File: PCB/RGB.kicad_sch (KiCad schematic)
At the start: 30 parts

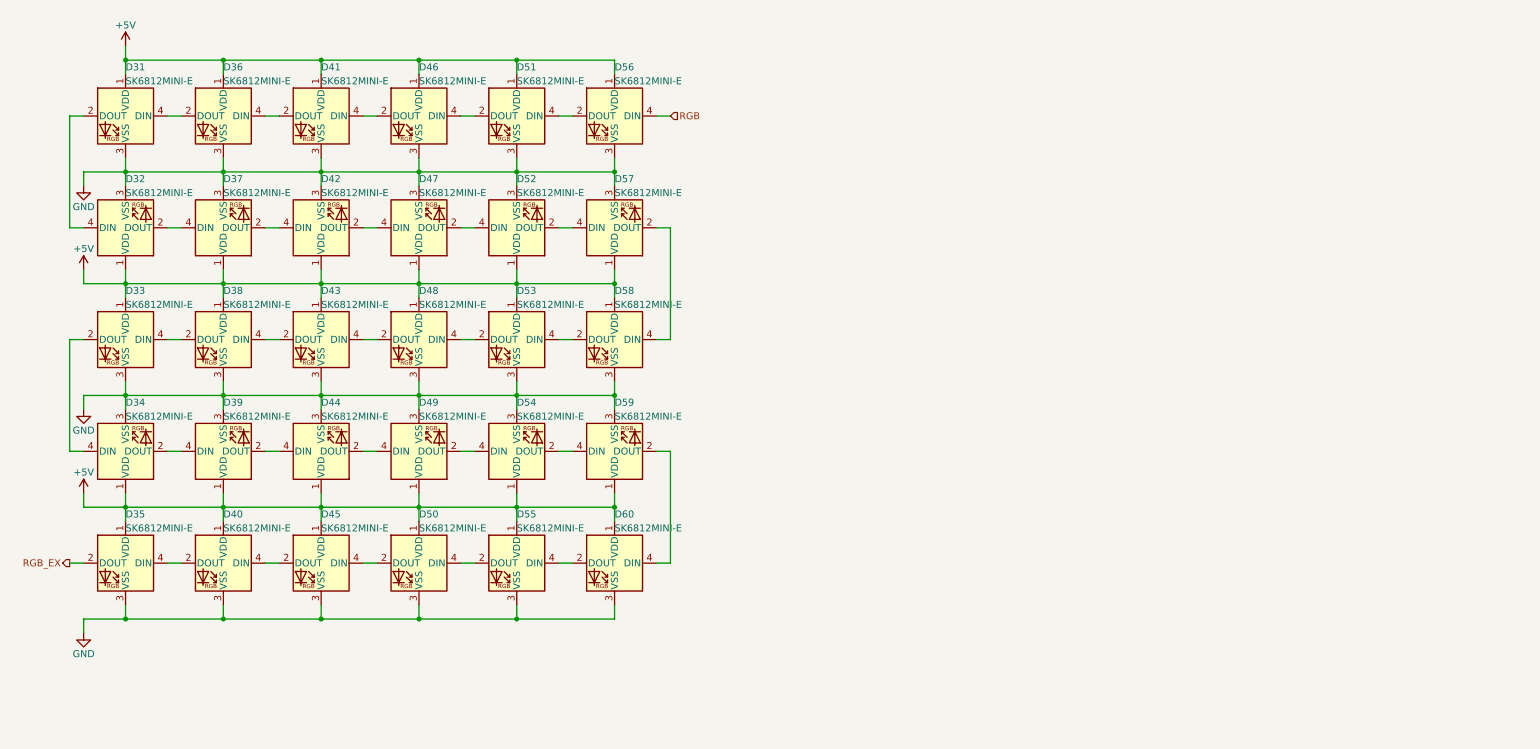
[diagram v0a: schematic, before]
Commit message: 08/08/2023 update
Removed Ogen footprint, and future VIK support is planned. Rerouted board following latest Honeydew revision. WIP support for the USB2541 is added, but it's very tentative and not yet complete. Added CX70M-24P1 footprint.
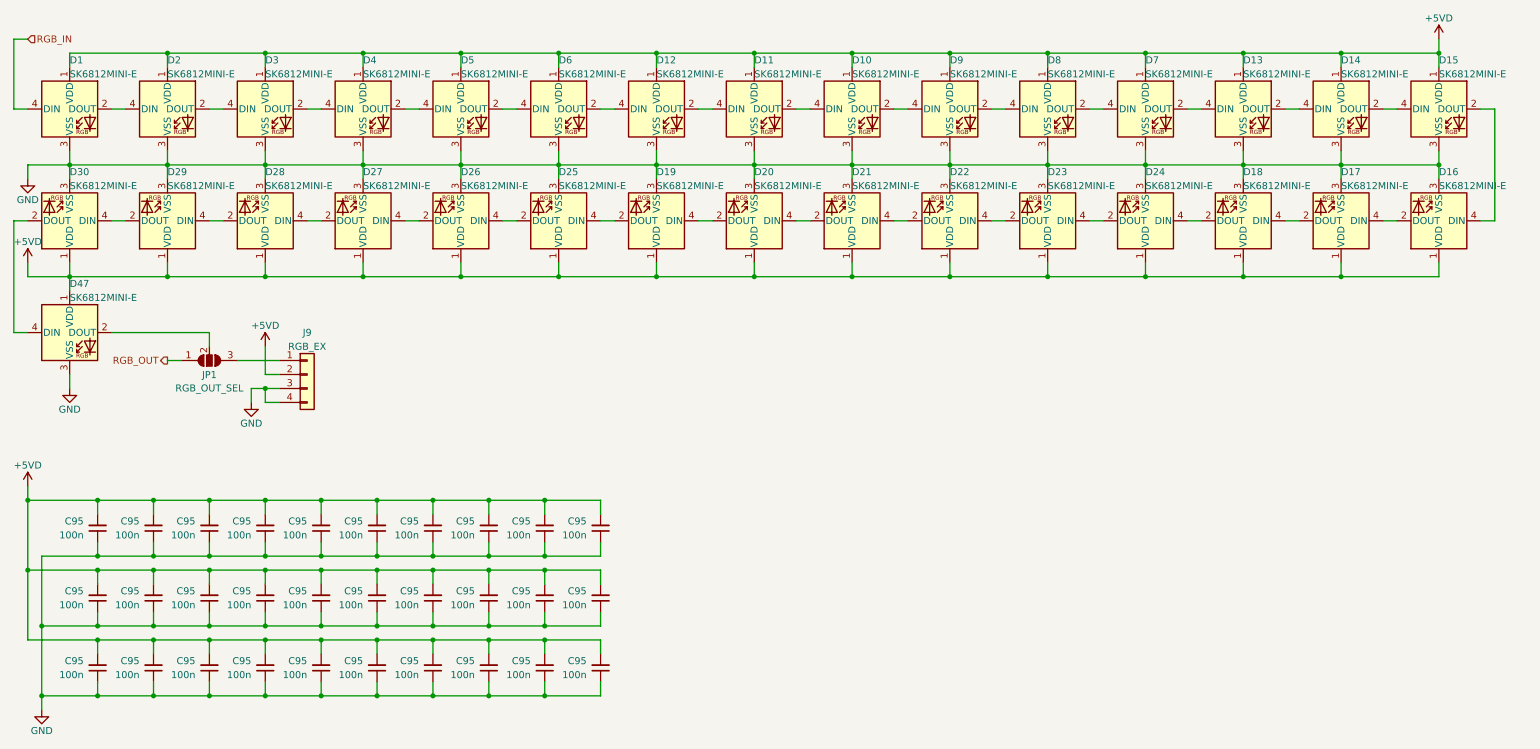
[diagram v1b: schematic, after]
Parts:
- removed D31, D32, D33, D34, D35, D36, D37, D38, D39, D40, D41, D42, D43, D44, D45, D46, D48, D49, D50, D51, D52, D53, D54, D55, D56, D57, D58, D59, D60: SK6812MINI-E, Cantaloupe:YS-SK6812MINI-E-Flippable, symbol Honeydew:SK6812MINI-E
- added C95 (x30): 100n, Cantaloupe:C_0402_1005Metric, symbol Device:C_Small
- added D1, D10, D11, D12, D13, D14, D15, D16, D17, D18, D19, D2, D20, D21, D22, D23, D24, D25, D26, D27, D28, D29, D3, D30, D4, D5, D6, D7, D8, D9: SK6812MINI-E, Cantaloupe:YS-SK6812MINI-E, symbol Honeydew:SK6812MINI-E
- added J9: RGB_EX, Cantaloupe:Header_RGB, symbol Connector_Generic:Conn_01x04
- added JP1: RGB_OUT_SEL, Jumper:SolderJumper-3_P1.3mm_Open_Pad1.0x1.5mm_NumberLabels, symbol Honeydew:SolderJumper_3_Open
- D47: footprint Cantaloupe:YS-SK6812MINI-E-Flippable -> Cantaloupe:YS-SK6812MINI-E; LCSC C5149201 -> C524051
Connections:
- net GND: now also C95.1, C95.1, C95.1, C95.1, C95.1, C95.1, C95.1, C95.1, C95.1, C95.1, C95.1, C95.1, C95.1, C95.1, C95.1, C95.1, C95.1, C95.1, C95.1, C95.1, C95.1, C95.1, C95.1, C95.1, C95.1, C95.1, C95.1, C95.1, C95.1, C95.1, D1.3 (VSS), D10.3 (VSS), D11.3 (VSS), D12.3 (VSS), D13.3 (VSS), D14.3 (VSS), D15.3 (VSS), D16.3 (VSS), D17.3 (VSS), D18.3 (VSS), D19.3 (VSS), D2.3 (VSS), D20.3 (VSS), D21.3 (VSS), D22.3 (VSS), D23.3 (VSS), D24.3 (VSS), D25.3 (VSS), D26.3 (VSS), D27.3 (VSS), D28.3 (VSS), D29.3 (VSS), D3.3 (VSS), D30.3 (VSS), D4.3 (VSS), D5.3 (VSS), D6.3 (VSS), D7.3 (VSS), D8.3 (VSS), D9.3 (VSS), J9.3 (Pin_3), J9.4 (Pin_4)
- net at D47.2 (DOUT): now also JP1.2 (C)
- net at D47.4 (DIN): now also D30.2 (DOUT)
- net +5V renamed +5VD
- net +5VD: now also C95.2, C95.2, C95.2, C95.2, C95.2, C95.2, C95.2, C95.2, C95.2, C95.2, C95.2, C95.2, C95.2, C95.2, C95.2, C95.2, C95.2, C95.2, C95.2, C95.2, C95.2, C95.2, C95.2, C95.2, C95.2, C95.2, C95.2, C95.2, C95.2, C95.2, D1.1 (VDD), D10.1 (VDD), D11.1 (VDD), D12.1 (VDD), D13.1 (VDD), D14.1 (VDD), D15.1 (VDD), D16.1 (VDD), D17.1 (VDD), D18.1 (VDD), D19.1 (VDD), D2.1 (VDD), D20.1 (VDD), D21.1 (VDD), D22.1 (VDD), D23.1 (VDD), D24.1 (VDD), D25.1 (VDD), D26.1 (VDD), D27.1 (VDD), D28.1 (VDD), D29.1 (VDD), D3.1 (VDD), D30.1 (VDD), D4.1 (VDD), D5.1 (VDD), D6.1 (VDD), D7.1 (VDD), D8.1 (VDD), D9.1 (VDD), J9.2 (Pin_2)
- new net: D19.4 (DIN), D20.2 (DOUT)
- new net: D20.4 (DIN), D21.2 (DOUT)
- new net: D26.2 (DOUT), D27.4 (DIN)
- new net: D25.2 (DOUT), D26.4 (DIN)
- new net: D2.2 (DOUT), D3.4 (DIN)
- new net: D1.2 (DOUT), D2.4 (DIN)
- new net: D16.2 (DOUT), D17.4 (DIN)
- new net: D15.2 (DOUT), D16.4 (DIN)
- new net: D4.2 (DOUT), D5.4 (DIN)
- new net: D3.2 (DOUT), D4.4 (DIN)
- new net: D21.4 (DIN), D22.2 (DOUT)
- new net: J9.1 (Pin_1), JP1.3 (B)
- new net: D28.2 (DOUT), D29.4 (DIN)
- new net: D27.2 (DOUT), D28.4 (DIN)
- new net: D12.4 (DIN), D6.2 (DOUT)
- new net: D5.2 (DOUT), D6.4 (DIN)
- new net: D8.4 (DIN), D9.2 (DOUT)
- new net: D10.2 (DOUT), D9.4 (DIN)
- new net: D22.4 (DIN), D23.2 (DOUT)
- new net: D19.2 (DOUT), D25.4 (DIN)
- new net: D13.4 (DIN), D7.2 (DOUT)
- new net: D7.4 (DIN), D8.2 (DOUT)
- new net: D11.4 (DIN), D12.2 (DOUT)
- new net: D14.2 (DOUT), D15.4 (DIN)
- new net: D13.2 (DOUT), D14.4 (DIN)
- new net: D23.4 (DIN), D24.2 (DOUT)
- new net: D18.2 (DOUT), D24.4 (DIN)
- new net: D29.2 (DOUT), D30.4 (DIN)
- new net: D17.2 (DOUT), D18.4 (DIN)
- new net: D10.4 (DIN), D11.2 (DOUT)
- new net RGB_IN: D1.4 (DIN)
- new net RGB_OUT: JP1.1 (A)
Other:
- company: (none) -> Created by Ariamelon (https://github.com/Ariamelon/Cantaloupe/)
- title: (none) -> Cantaloupe split ergonomic keyboard
